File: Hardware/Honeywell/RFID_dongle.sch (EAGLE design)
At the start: 13 parts, among them J1 USB_B_PTH, J5 1X2-3.5MM, J6 1X2-3.5MM, U1 4MB Flash

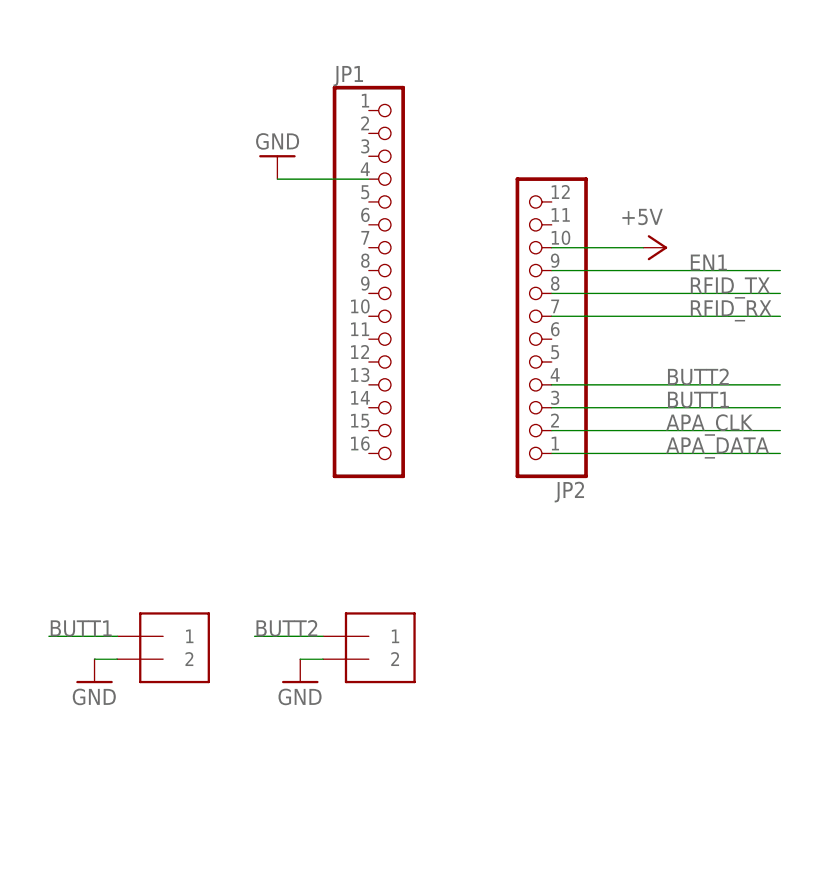
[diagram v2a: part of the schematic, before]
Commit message: HEEP-878 updated honeywell pcb for allpcb fab, swapped button GPIO
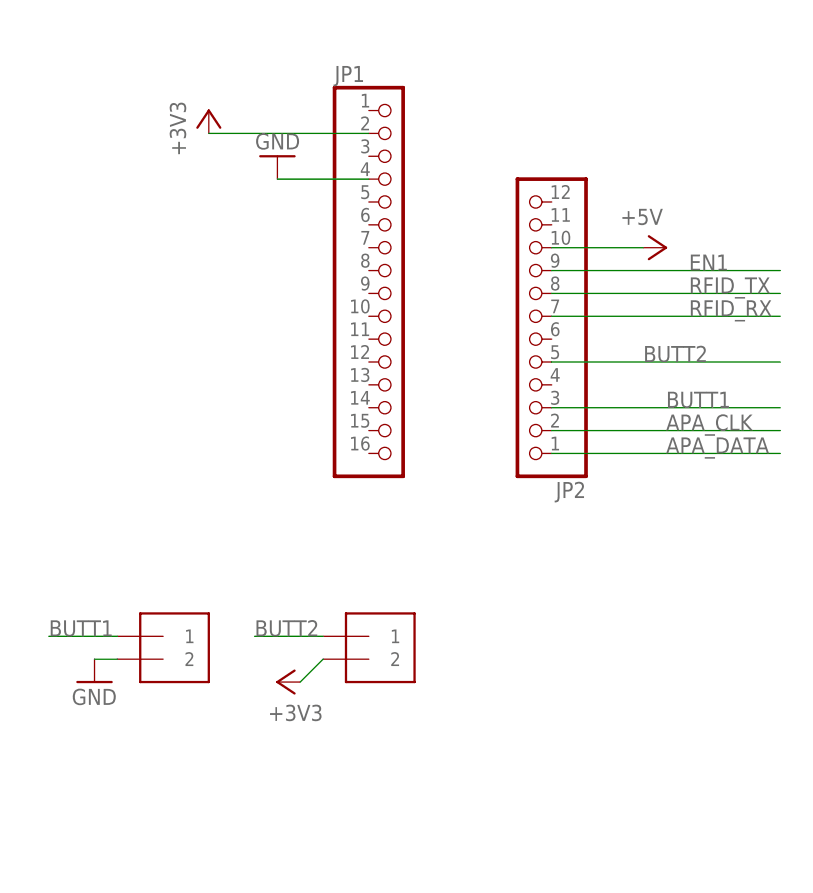
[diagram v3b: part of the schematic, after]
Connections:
- new net +3V3: J6.2, JP1.2
- net BUTT2: now also JP2.5; no longer JP2.4
- net GND: no longer J6.2
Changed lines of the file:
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@@
 <grid distance="0.1" unitdist="inch" unit="inch" style="lines" multiple="1" display="no" altdistance="0.01" altunitdist="inch" altunit="inch"/>
 <layers>
-<layer number="1" name="Top" color="4" fill="1" visible="yes" active="no"/>
-<layer number="16" name="Bottom" color="1" fill="1" visible="yes" active="no"/>
-<layer number="17" name="Pads" color="2" fill="1" visible="yes" active="no"/>
-<layer number="18" name="Vias" color="2" fill="1" visible="yes" active="no"/>
-<layer number="19" name="Unrouted" color="6" fill="1" visible="yes" active="no"/>
-<layer number="20" name="Dimension" color="24" fill="1" visible="yes" active="no"/>
-<layer number="21" name="tPlace" color="7" fill="1" visible="yes" active="no"/>
-<layer number="22" name="bPlace" color="7" fill="1" visible="yes" active="no"/>
-<layer number="23" name="tOrigins" color="15" fill="1" visible="yes" active="no"/>
-<layer number="24" name="bOrigins" color="15" fill="1" visible="yes" active="no"/>
-<layer number="25" name="tNames" color="7" fill="1" visible="yes" active="no"/>
-<layer number="26" name="bNames" color="7" fill="1" visible="yes" active="no"/>
-<layer number="27" name="tValues" color="7" fill="1" visible="yes" active="no"/>
-<layer number="28" name="bValues" color="7" fill="1" visible="yes" active="no"/>
+<layer number="1" name="Top" color="4" fill="1" visible="no" active="no"/>
+<layer number="16" name="Bottom" color="1" fill="1" visible="no" active="no"/>
+<layer number="17" name="Pads" color="2" fill="1" visible="no" active="no"/>
+<layer number="18" name="Vias" color="2" fill="1" visible="no" active="no"/>
+<layer number="19" name="Unrouted" color="6" fill="1" visible="no" active="no"/>
+<layer number="20" name="Dimension" color="24" fill="1" visible="no" active="no"/>
+<layer number="21" name="tPlace" color="7" fill="1" visible="no" active="no"/>
+<layer number="22" name="bPlace" color="7" fill="1" visible="no" active="no"/>
+<layer number="23" name="tOrigins" color="15" fill="1" visible="no" active="no"/>
+<layer number="24" name="bOrigins" color="15" fill="1" visible="no" active="no"/>
+<layer number="25" name="tNames" color="7" fill="1" visible="no" active="no"/>
+<layer number="26" name="bNames" color="7" fill="1" visible="no" active="no"/>
+<layer number="27" name="tValues" color="7" fill="1" visible="no" active="no"/>
+<layer number="28" name="bValues" color="7" fill="1" visible="no" active="no"/>
 <layer number="29" name="tStop" color="7" fill="3" visible="no" active="no"/>
 <layer number="30" name="bStop" color="7" fill="6" visible="no" active="no"/>
@@
 <layer number="35" name="tGlue" color="7" fill="4" visible="no" active="no"/>
 <layer number="36" name="bGlue" color="7" fill="5" visible="no" active="no"/>
-<layer number="37" name="tTest" color="7" fill="1" visible="yes" active="no"/>
-<layer number="38" name="bTest" color="7" fill="1" visible="yes" active="no"/>
+<layer number="37" name="tTest" color="7" fill="1" visible="no" active="no"/>
+<layer number="38" name="bTest" color="7" fill="1" visible="no" active="no"/>
 <layer number="39" name="tKeepout" color="4" fill="11" visible="no" active="no"/>
 <layer number="40" name="bKeepout" color="1" fill="11" visible="no" active="no"/>
@@
 <layer number="44" name="Drills" color="7" fill="1" visible="no" active="no"/>
 <layer number="45" name="Holes" color="7" fill="1" visible="no" active="no"/>
-<layer number="46" name="Milling" color="3" fill="1" visible="yes" active="no"/>
-<layer number="47" name="Measures" color="7" fill="1" visible="yes" active="no"/>
-<layer number="48" name="Document" color="7" fill="1" visible="yes" active="no"/>
-<layer number="49" name="Reference" color="7" fill="1" visible="yes" active="no"/>
-<layer number="50" name="dxf" color="7" fill="1" visible="yes" active="no"/>
-<layer number="51" name="tDocu" color="7" fill="1" visible="yes" active="no"/>
-<layer number="52" name="bDocu" color="7" fill="1" visible="yes" active="no"/>
-<layer number="53" name="tGND_GNDA" color="7" fill="9" visible="yes" active="no"/>
-<layer number="54" name="bGND_GNDA" color="1" fill="9" visible="yes" active="no"/>
-<layer number="56" name="wert" color="7" fill="1" visible="yes" active="no"/>
-<layer number="57" name="tCAD" color="7" fill="1" visible="yes" active="no"/>
-<layer number="59" name="tCarbon" color="7" fill="1" visible="yes" active="no"/>
-<layer number="60" name="bCarbon" color="7" fill="1" visible="yes" active="no"/>
+<layer number="46" name="Milling" color="3" fill="1" visible="no" active="no"/>
+<layer number="47" name="Measures" color="7" fill="1" visible="no" active="no"/>
+<layer number="48" name="Document" color="7" fill="1" visible="no" active="no"/>
+<layer number="49" name="Reference" color="7" fill="1" visible="no" active="no"/>
+<layer number="50" name="dxf" color="7" fill="1" visible="no" active="no"/>
+<layer number="51" name="tDocu" color="7" fill="1" visible="no" active="no"/>
+<layer number="52" name="bDocu" color="7" fill="1" visible="no" active="no"/>
+<layer number="53" name="tGND_GNDA" color="7" fill="9" visible="no" active="no"/>
+<layer number="54" name="bGND_GNDA" color="1" fill="9" visible="no" active="no"/>
+<layer number="56" name="wert" color="7" fill="1" visible="no" active="no"/>
+<layer number="57" name="tCAD" color="7" fill="1" visible="no" active="no"/>
+<layer number="59" name="tCarbon" color="7" fill="1" visible="no" active="no"/>
+<layer number="60" name="bCarbon" color="7" fill="1" visible="no" active="no"/>
 <layer number="88" name="SimResults" color="9" fill="1" visible="yes" active="yes"/>
 <layer number="89" name="SimProbes" color="9" fill="1" visible="yes" active="yes"/>
@@
 <part name="J6" library="adafruit" deviceset="1X2" device="-3.5MM"/>
 <part name="GND3" library="SparkFun-Aesthetics" deviceset="GND" device=""/>
-<part name="GND6" library="SparkFun-Aesthetics" deviceset="GND" device=""/>
 <part name="GND7" library="SparkFun-Aesthetics" deviceset="GND" device=""/>
 <part name="P+5" library="supply1" library_urn="urn:adsk.eagle:library:371" deviceset="+5V" device=""/>
@@
 <part name="GND11" library="SparkFun-Aesthetics" deviceset="GND" device=""/>
 <part name="GND12" library="supply1" library_urn="urn:adsk.eagle:library:371" deviceset="GND" device=""/>
+<part name="+3V1" library="supply1" library_urn="urn:adsk.eagle:library:371" deviceset="+3V3" device=""/>
+<part name="+3V2" library="supply1" library_urn="urn:adsk.eagle:library:371" deviceset="+3V3" device=""/>
 </parts>
 <sheets>
@@
 <instance part="J6" gate="G$1" x="137.16" y="-10.16"/>
 <instance part="GND3" gate="1" x="106.68" y="-12.7"/>
-<instance part="GND6" gate="1" x="129.54" y="-12.7"/>
 <instance part="GND7" gate="1" x="78.74" y="-43.18"/>
 <instance part="P+5" gate="1" x="78.74" y="-20.32"/>
@@
 <instance part="GND11" gate="1" x="0" y="-40.64"/>
 <instance part="GND12" gate="1" x="27.94" y="40.64"/>
+<instance part="+3V1" gate="G$1" x="119.38" y="50.8"/>
+<instance part="+3V2" gate="G$1" x="127" y="-12.7" rot="R90"/>
 </instances>
 <busses>
@@
 <pinref part="GND3" gate="1" pin="GND"/>
 <wire x1="106.68" y1="-10.16" x2="109.22" y2="-10.16" width="0.1524" layer="91"/>
-</segment>
-<segment>
-<pinref part="J6" gate="G$1" pin="2"/>
-<pinref part="GND6" gate="1" pin="GND"/>
-<wire x1="129.54" y1="-10.16" x2="132.08" y2="-10.16" width="0.1524" layer="91"/>
 </segment>
 <segment>
@@
 </segment>
 <segment>
-<pinref part="JP2" gate="G$1" pin="4"/>
-<wire x1="157.48" y1="20.32" x2="182.88" y2="20.32" width="0.1524" layer="91"/>
-<label x="170.18" y="20.32" size="1.778" layer="95"/>
+<wire x1="157.48" y1="22.86" x2="182.88" y2="22.86" width="0.1524" layer="91"/>
+<label x="167.64" y="22.86" size="1.778" layer="95"/>
+<pinref part="JP2" gate="G$1" pin="5"/>
 </segment>
 </net>
@@
 </segment>
 </net>
+<net name="+3V3" class="0">
+<segment>
+<pinref part="J6" gate="G$1" pin="2"/>
+<wire x1="129.54" y1="-12.7" x2="132.08" y2="-10.16" width="0.1524" layer="91"/>
+<pinref part="+3V2" gate="G$1" pin="+3V3"/>
+</segment>
+<segment>
+<pinref part="JP1" gate="A" pin="2"/>
+<pinref part="+3V1" gate="G$1" pin="+3V3"/>
+<wire x1="119.38" y1="48.26" x2="137.16" y2="48.26" width="0.1524" layer="91"/>
+</segment>
+</net>
